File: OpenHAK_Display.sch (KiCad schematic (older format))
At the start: 10 parts, among them P1 CONN_01X08

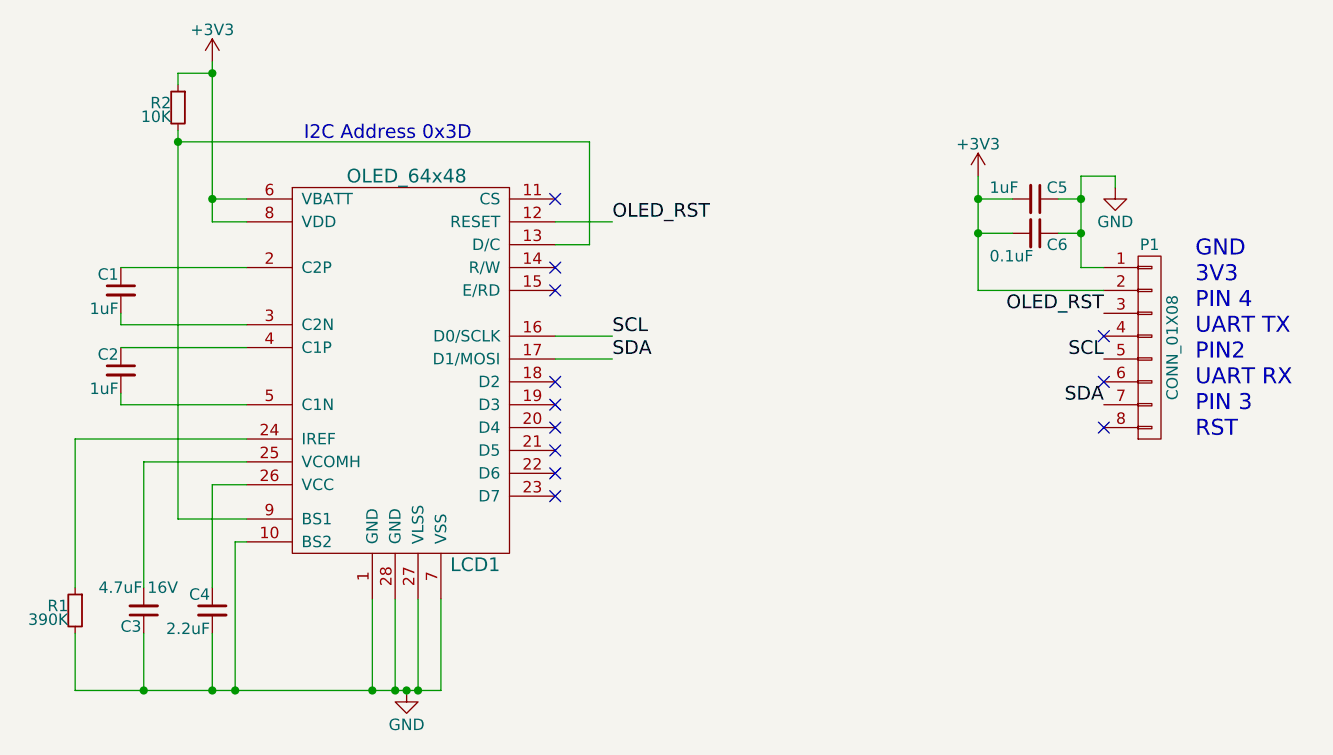
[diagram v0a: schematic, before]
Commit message: Connect pin 17 to pin 18 to make it work
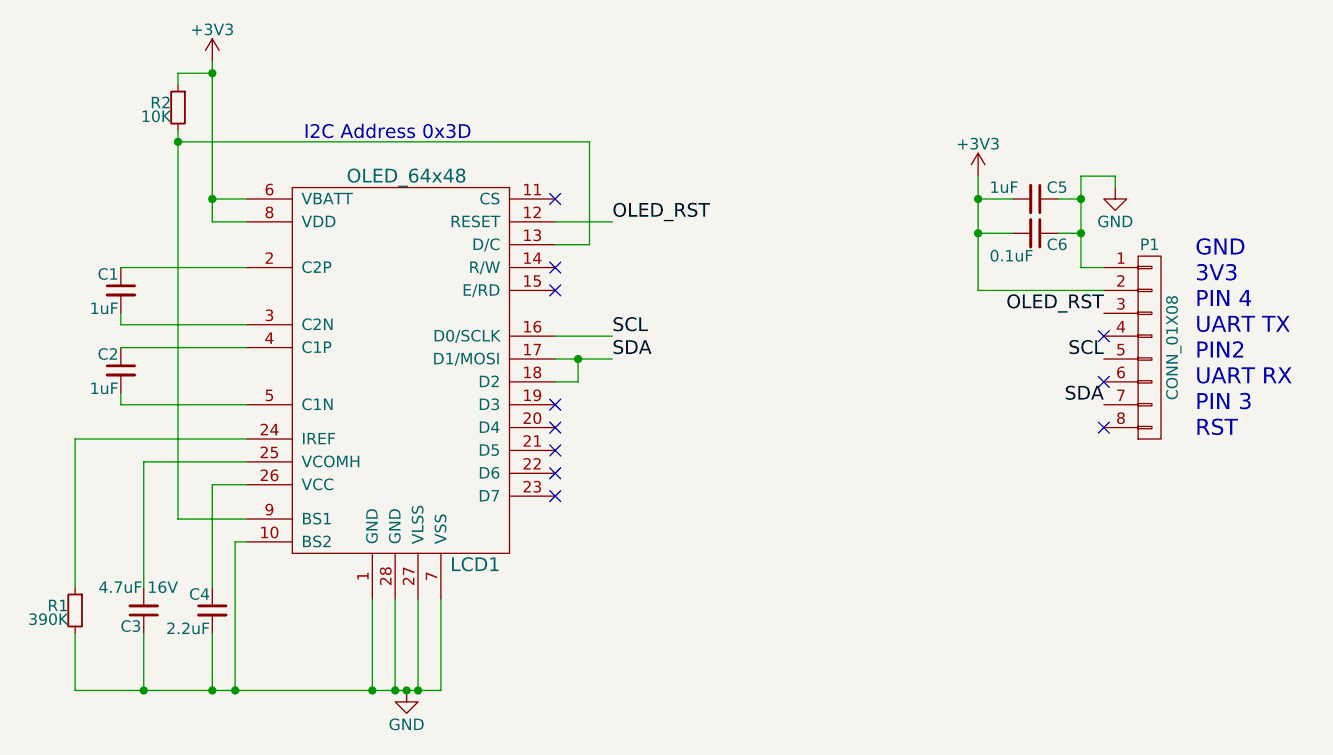
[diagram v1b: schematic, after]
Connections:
- net SDA: now also LCD1.18 (D2)
- no-connect marks 12 -> 11
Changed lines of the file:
@@
 NoConn ~ 5050 3300
 NoConn ~ 5050 3400
-NoConn ~ 5050 3800
 NoConn ~ 5050 3900
 NoConn ~ 5050 4000
@@
 	7250 3150 7350 3150
 Connection ~ 7350 3150
+Wire Wire Line
+	5050 3800 5150 3800
+Wire Wire Line
+	5150 3800 5150 3700
+Connection ~ 5150 3700
 $EndSCHEMATC
